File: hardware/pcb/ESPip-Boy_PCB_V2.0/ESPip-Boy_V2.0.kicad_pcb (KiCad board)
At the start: 4 copper layers, 37 x 31.1 mm, 106 parts, among them CN1 1X4, Q1 SS8050/Y1, Q2 SS8050/Y1, Q3 DMG1012T-7, Q4 DMG1012T-7, Q5 SS8050/Y1, SW1 SW-SMD_L4.7-W3.5-P3.35-EH, SW2 SW-SMD_L4.7-W3.5-P3.35-EH, U1 LTR-390UV-01, U10 ICS-43434_C5656610, U11 ME6217A33PG, U12 BQ24074RGTR, U13 MAX30102EFD+T_C6454833, U14 BQ27421YZFR-G1A, U17 MAX98357AETE+T, U18 ME6206B18XG, U2 CP2102N-A02-GQFN28R, U3 0402 Blue, U4 GT-USB-7010ASV, U5 BMI270, U7 YSN8010SJ 32.768KHZ, U8 ESP32-WROOM-32E(8MB), U9 LIS2MDLTR

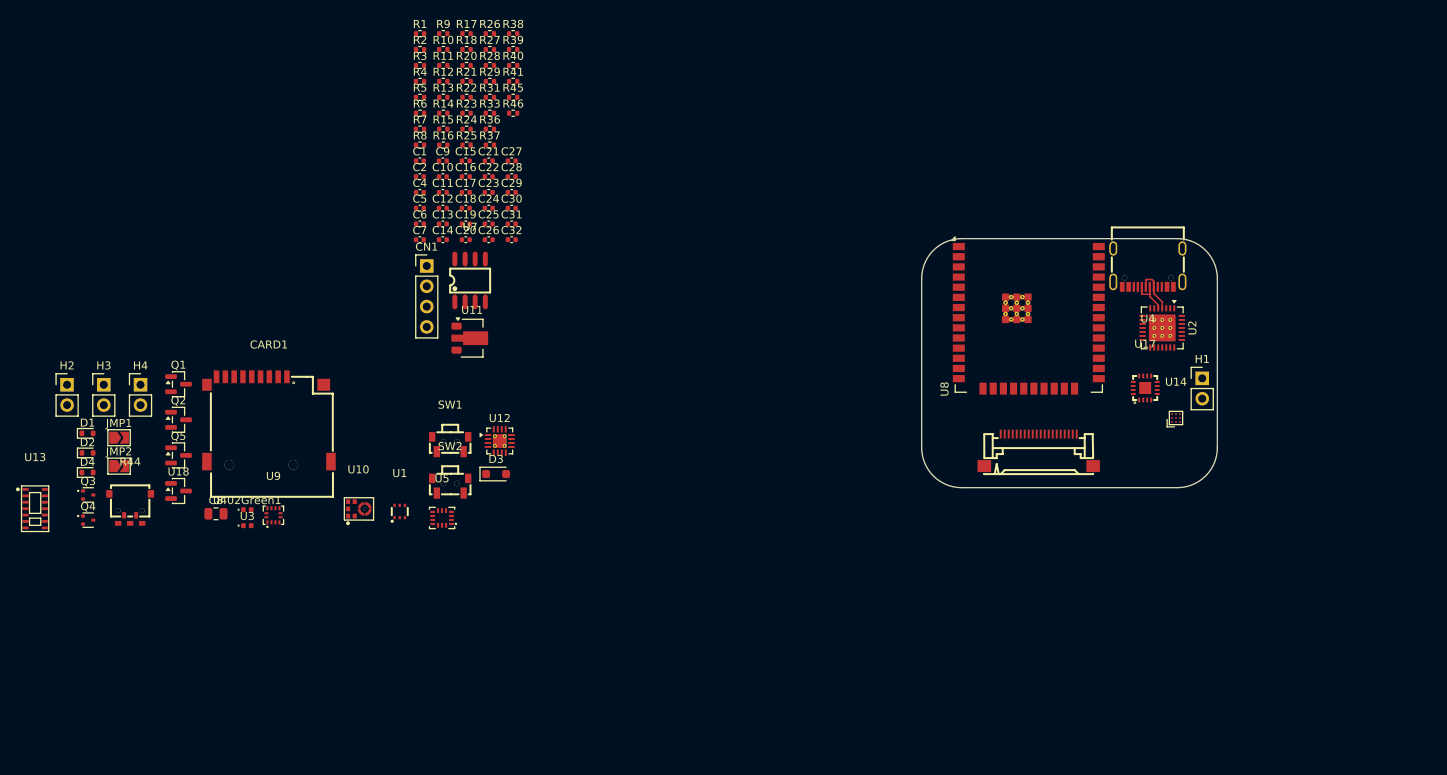
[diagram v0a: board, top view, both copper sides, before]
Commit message: Placed some more components for V2.0
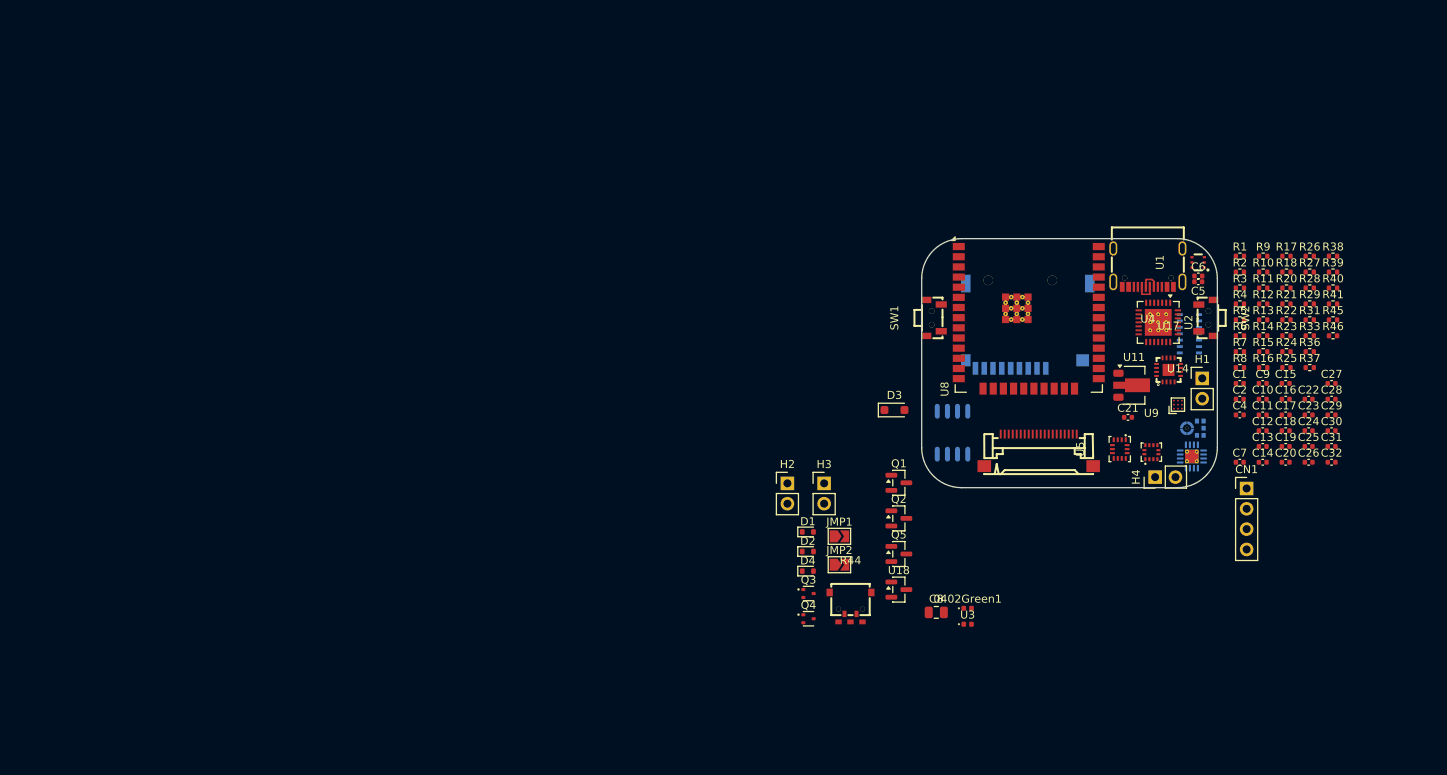
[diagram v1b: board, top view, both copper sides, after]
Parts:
- CARD1, U10, U12, U13, U7: moved to B.Cu
- moved U13 145.9 mm to (180.6, 70.9), turned to 180 degrees
- moved H4 127.4 mm to (176.3, 88.8), turned to 90 degrees
- moved U9 110.0 mm to (175.8, 85.7)
- moved C10 106.2 mm to (189.8, 79.1)
- moved C11 106.2 mm to (189.8, 81.0)
- moved C12 106.2 mm to (189.8, 83.0)
- moved C13 106.2 mm to (189.8, 85.0)
- moved C14 106.2 mm to (189.8, 86.9)
- moved C9 106.2 mm to (189.8, 77.1)
- moved R10 106.2 mm to (189.8, 63.2)
- moved R11 106.2 mm to (189.8, 65.2)
- moved R12 106.2 mm to (189.8, 67.2)
- moved R13 106.2 mm to (189.8, 69.1)
- moved R14 106.2 mm to (189.8, 71.1)
- moved R15 106.2 mm to (189.8, 73.1)
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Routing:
- net USB_DP: track 5.84 -> 2.68 mm
- net USB_DN: track 5.27 -> 2.81 mm

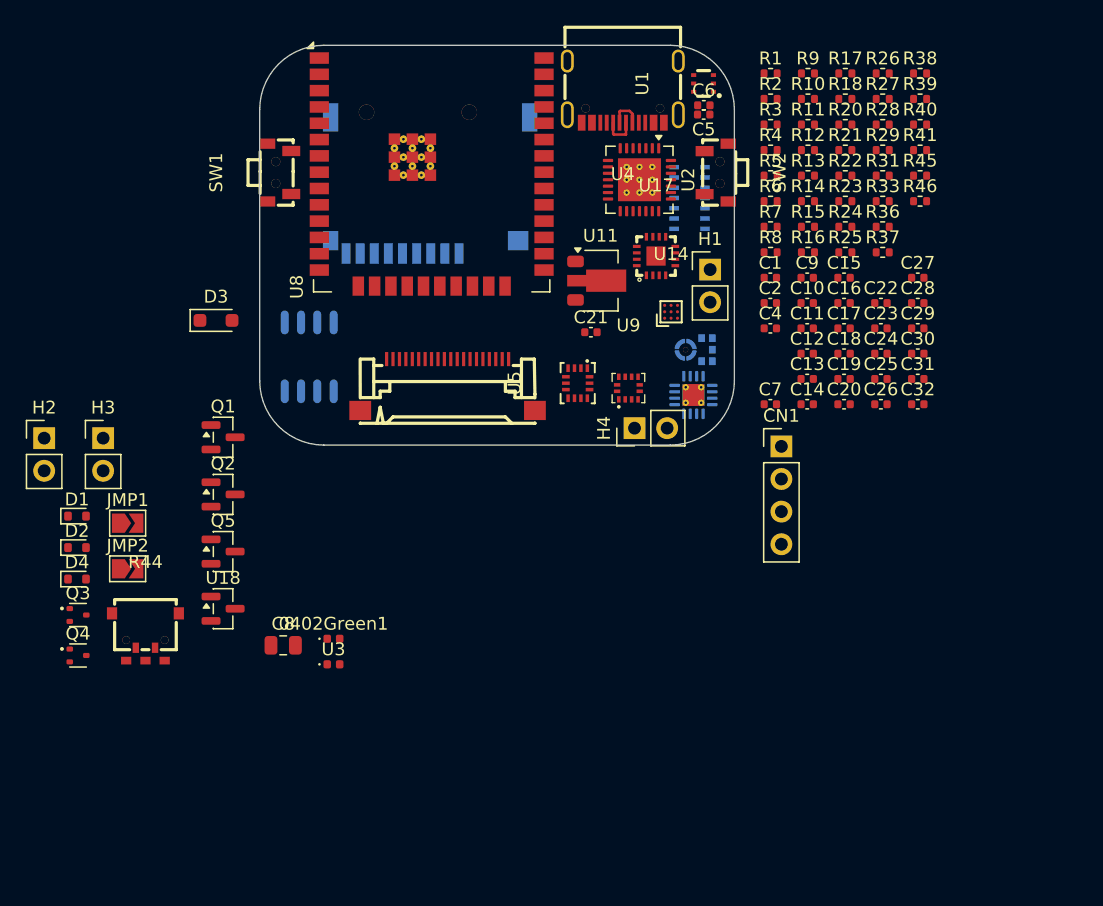
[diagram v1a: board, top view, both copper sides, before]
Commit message: V2.0 finished. All hardware verified, only motor and microphone not working as expected
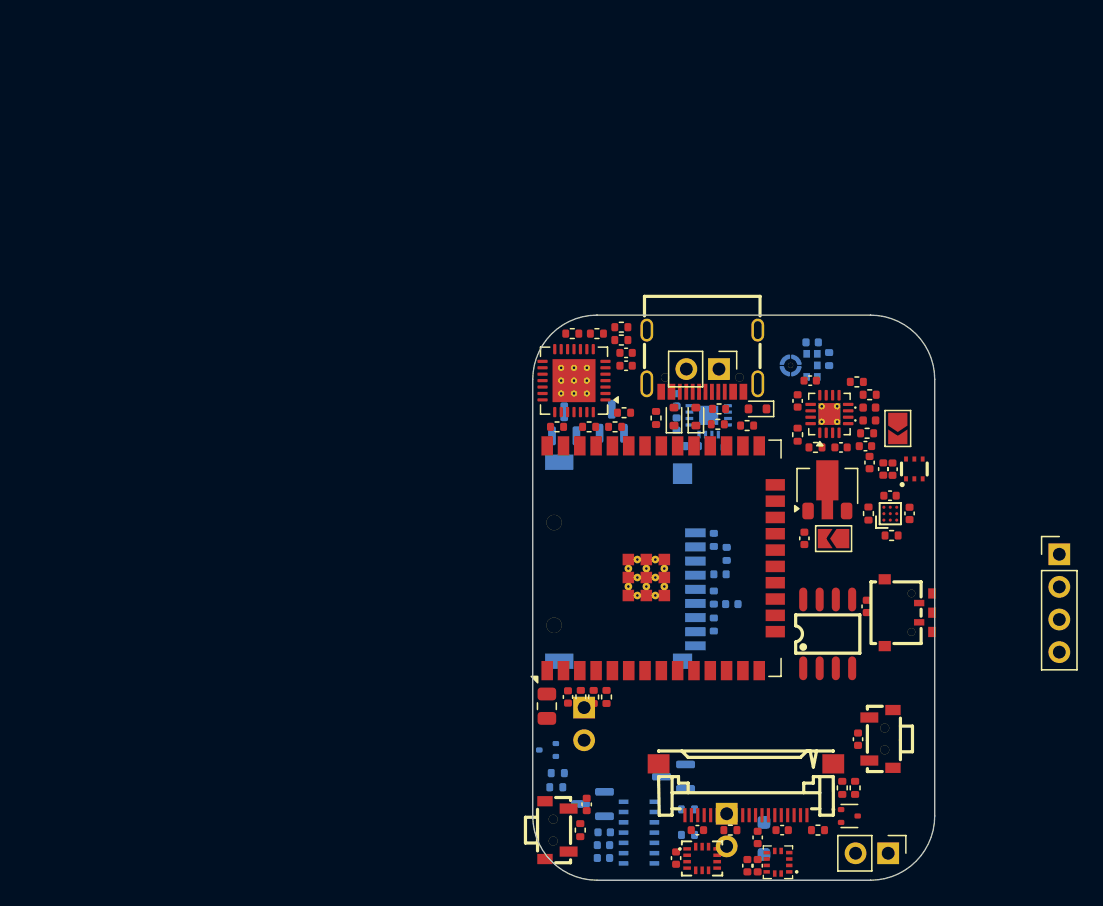
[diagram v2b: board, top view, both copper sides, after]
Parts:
- added U6: ~, 1_custom_fp_lib:200_mah_lipo, B.Cu at (193.8, 100.2)
- C10, C12, C13, C16, C17, C19, C30, C32, D3, H2, H3, Q1, Q2, Q4, Q5, R15, R20, R21, R22, R23, R24, R31, R33, R38, R39, R46, U17, U18: moved to B.Cu
- U12, U7: moved to F.Cu
- moved Q3 62.1 mm to (193.1, 119.0)
- moved H2 60.7 mm to (183.5, 118.8), turned to 180 degrees
- moved JMP1 60.4 mm to (196.8, 88.8), turned to -90 degrees
- moved R39 59.6 mm to (170.3, 115.7), turned to 180 degrees
- moved R44 59.4 mm to (197.6, 103.2), turned to 90 degrees
- moved R26 59.1 mm to (190.6, 120.1), turned to 180 degrees
- moved D3 58.7 mm to (186.4, 120.8), turned to -90 degrees
- moved R11 57.7 mm to (172.1, 120.1), turned to 90 degrees
- moved R28 56.2 mm to (183.8, 120.1)
- moved SW1 55.6 mm to (170.3, 120.1)
- moved JMP2 55.0 mm to (191.8, 97.4), turned to 180 degrees
- moved D2 54.1 mm to (185.9, 87.3), turned to 180 degrees
- moved R27 53.7 mm to (192.5, 116.8), turned to 90 degrees
- moved R46 53.7 mm to (170.2, 116.8), turned to 180 degrees
- moved R18 53.6 mm to (193.5, 116.8), turned to 90 degrees
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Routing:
- net USB_DN: track 2.81 -> 0.00 mm
- net USB_DP: track 2.68 -> 0.00 mm
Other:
- board size 37 x 31.1 mm -> 31.3 x 44 mm
